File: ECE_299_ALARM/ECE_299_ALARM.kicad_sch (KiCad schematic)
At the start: 16 parts, among them SW1 SW_Push_Dual, SW2 SW_Push_Dual, SW3 SW_Push_Dual, SW4 SW_Push_Dual, U1 RDA5807M_Module, U2 RPi_Pico_TH, U3 LM386

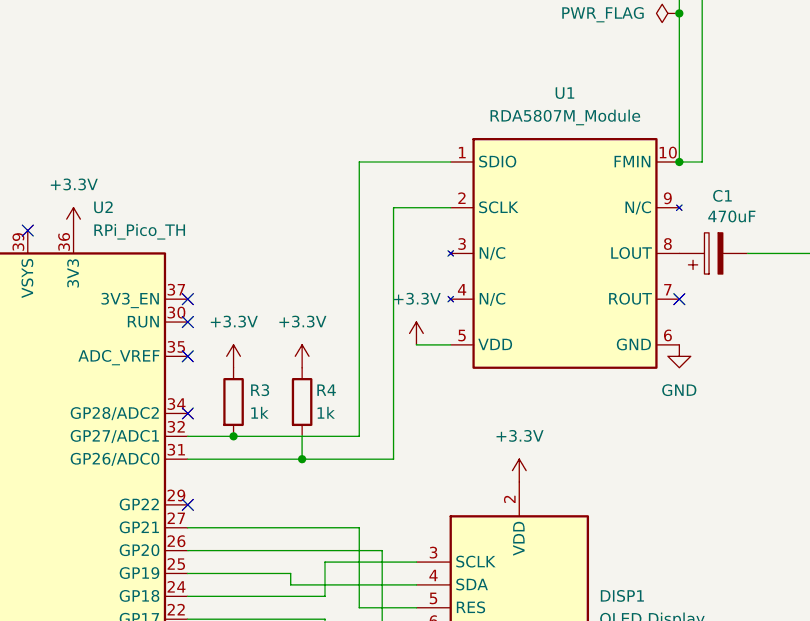
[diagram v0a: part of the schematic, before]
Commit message: fix swapped SDA and SCL on radio module
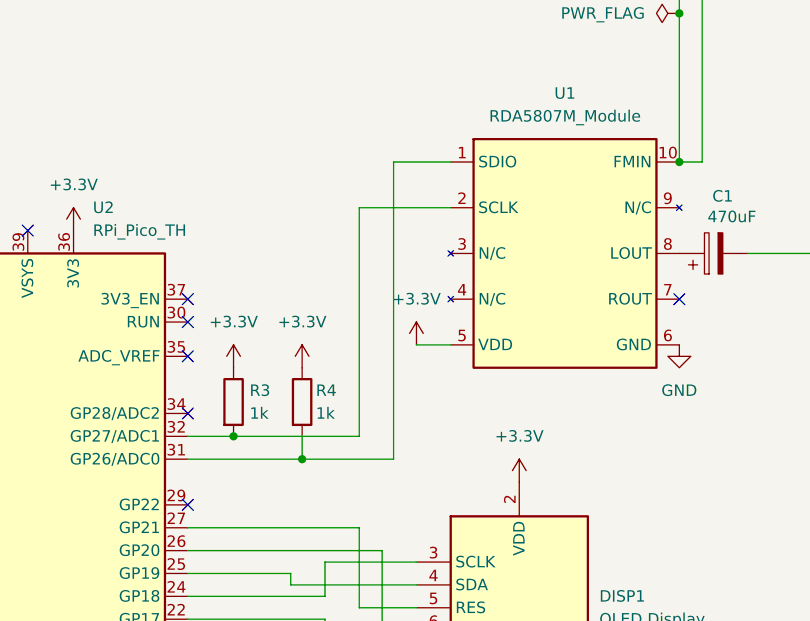
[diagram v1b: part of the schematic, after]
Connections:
- net at R3.2, U2.32 (GP27/ADC1): now also U1.2 (SCLK); no longer U1.1 (SDIO)
- net at R4.2, U2.31 (GP26/ADC0): now also U1.1 (SDIO); no longer U1.2 (SCLK)
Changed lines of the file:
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@@
 	(wire
 		(pts
-			(xy 132.08 102.87) (xy 132.08 74.93)
+			(xy 132.08 69.85) (xy 132.08 102.87)
 		)
 		(stroke
@@
 	(wire
 		(pts
+			(xy 128.27 74.93) (xy 128.27 100.33)
+		)
+		(stroke
+			(width 0)
+			(type default)
+		)
+	)
+	(wire
+		(pts
 			(xy 130.81 121.92) (xy 134.62 121.92)
 		)
@@
 	(wire
 		(pts
+			(xy 128.27 74.93) (xy 138.43 74.93)
+		)
+		(stroke
+			(width 0)
+			(type default)
+		)
+	)
+	(wire
+		(pts
 			(xy 130.81 113.03) (xy 130.81 121.92)
 		)
@@
 	(wire
 		(pts
+			(xy 132.08 69.85) (xy 138.43 69.85)
+		)
+		(stroke
+			(width 0)
+			(type default)
+		)
+	)
+	(wire
+		(pts
 			(xy 128.27 110.49) (xy 128.27 119.38)
 		)
@@
 	(wire
 		(pts
-			(xy 132.08 74.93) (xy 138.43 74.93)
-		)
-		(stroke
-			(width 0)
-			(type default)
-		)
-	)
-	(wire
-		(pts
-			(xy 128.27 69.85) (xy 128.27 100.33)
-		)
-		(stroke
-			(width 0)
-			(type default)
-		)
-	)
-	(wire
-		(pts
 			(xy 238.76 90.17) (xy 251.46 90.17)
 		)
@@
 		)
 		(stroke
-			(width 0)
-			(type default)
-		)
-	)
-	(wire
-		(pts
-			(xy 128.27 69.85) (xy 138.43 69.85)
-		)
-		(stroke

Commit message: i just wasted an hour making better routing
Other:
- moved on the sheet: C1
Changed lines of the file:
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@@
 	(wire
 		(pts
-			(xy 171.45 80.01) (xy 212.09 80.01)
+			(xy 191.77 80.01) (xy 212.09 80.01)
 		)
 		(stroke
@@
 		(pts
 			(xy 109.22 113.03) (xy 130.81 113.03)
+		)
+		(stroke
+			(width 0)
+			(type default)
+		)
+	)
+	(wire
+		(pts
+			(xy 184.15 80.01) (xy 163.83 80.01)
 		)
 		(stroke
@@
 	(symbol
 		(lib_id "Device:C_Polarized")
-		(at 167.64 80.01 90)
+		(at 187.96 80.01 90)
 		(unit 1)
 		(exclude_from_sim no)
@@
 		(dnp no)
 		(property "Reference" "C1"
-			(at 168.656 73.66 90)
+			(at 188.976 73.66 90)
 			(effects
 				(font
@@
 		)
 		(property "Value" "470uF"
-			(at 169.672 75.946 90)
+			(at 189.992 75.946 90)
 			(effects
 				(font
@@
 		)
 		(property "Footprint" "Capacitor_THT:C_Radial_D6.3mm_H11.0mm_P2.50mm"
-			(at 171.45 79.0448 0)
+			(at 191.77 79.0448 0)
 			(effects
 				(font
@@
 		)
 		(property "Datasheet" "~"
-			(at 167.64 80.01 0)
+			(at 187.96 80.01 0)
 			(effects
 				(font
@@
 		)
 		(property "Description" "Polarized capacitor"
-			(at 167.64 80.01 0)
-			(effects
-				(font
+			(at 187.96 80.01 0)
+			(effects
+				(font

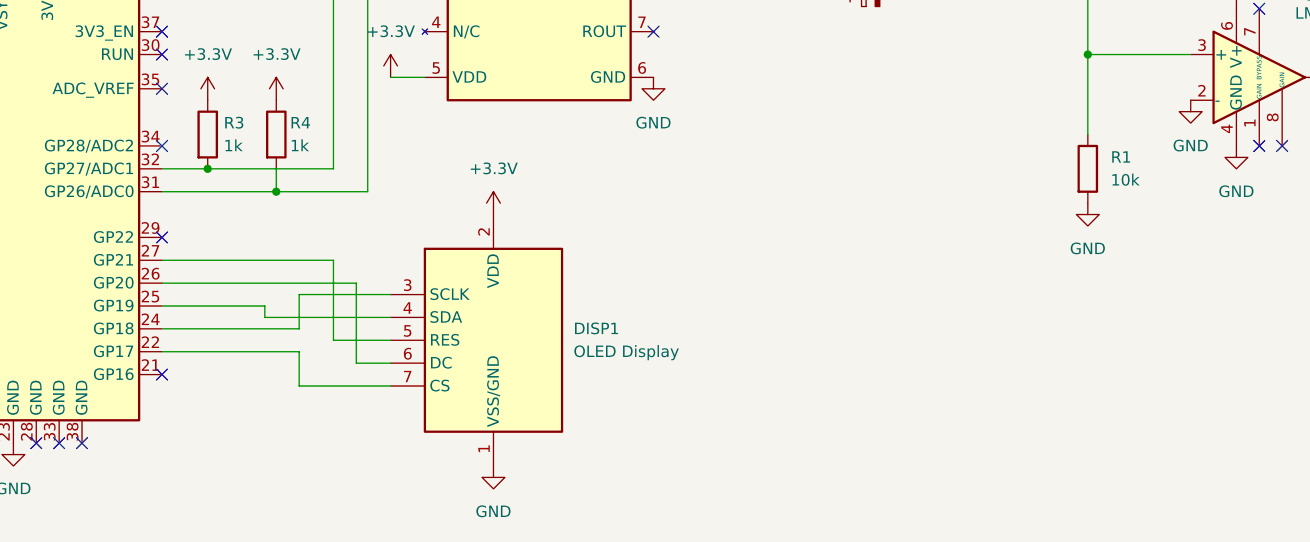
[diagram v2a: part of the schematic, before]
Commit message: add high current path, 1mm is probably excessive
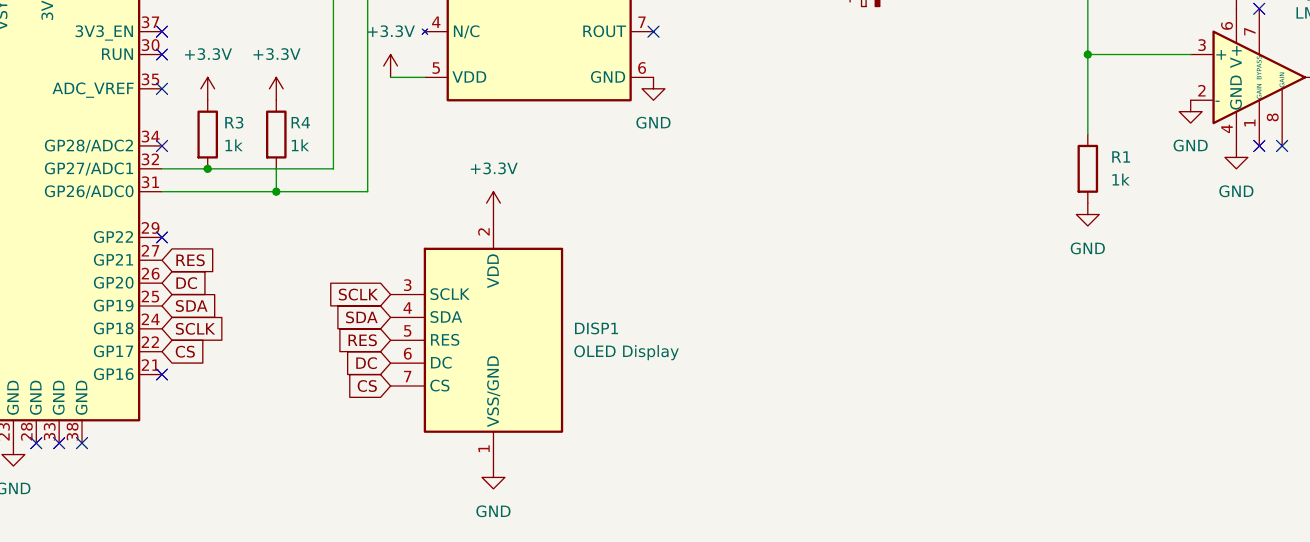
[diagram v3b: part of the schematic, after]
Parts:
- R1: value 10k -> 1k
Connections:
- net CS: now reaches DISP1.7 (CS), U2.22 (GP17)
- net SCLK: now reaches DISP1.3 (SCLK), U2.24 (GP18)
- net SDA: now reaches DISP1.4 (SDA), U2.25 (GP19)
- net DC: now reaches DISP1.6 (DC), U2.26 (GP20)
- net RES: now reaches DISP1.5 (RES), U2.27 (GP21)

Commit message: small_adjustments
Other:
- moved on the sheet: AE1, C1, C2, DISP1, LS1, R1, R2, R3, R4, SW1, SW2, SW3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
